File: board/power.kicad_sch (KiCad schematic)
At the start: 10 parts, among them U1 OKI-78SR-5_1.5-W36H-C

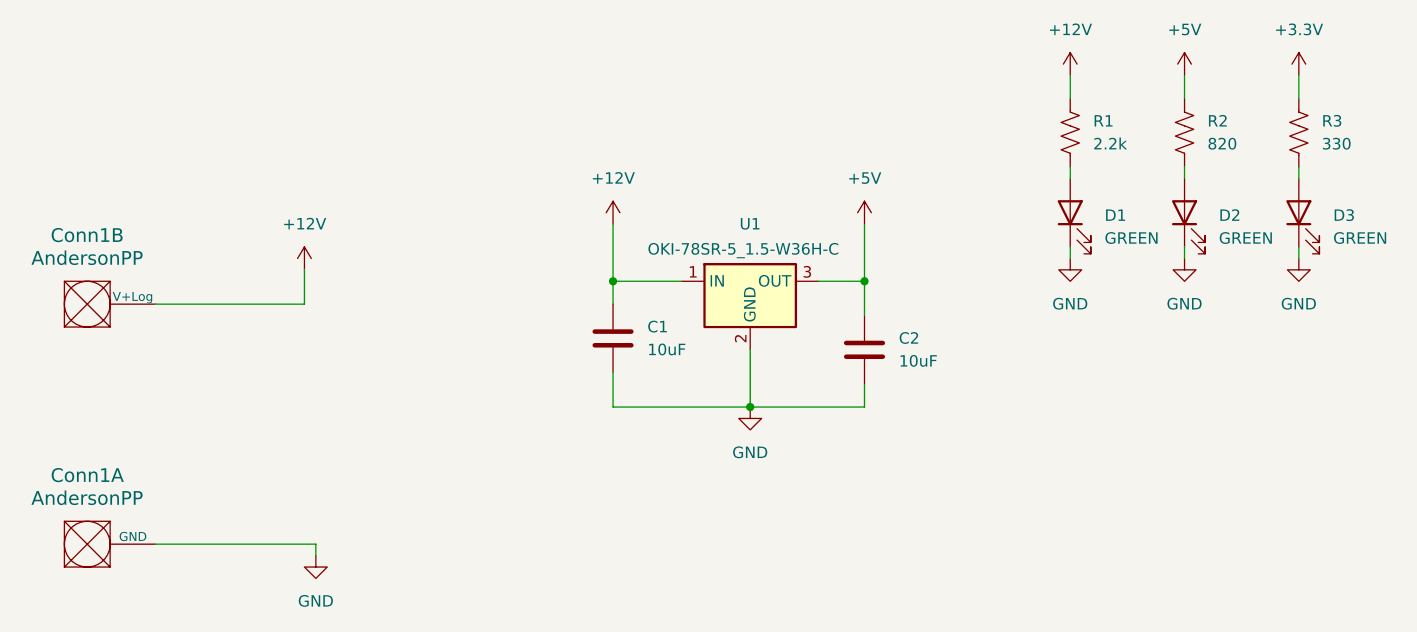
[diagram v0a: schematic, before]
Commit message: Added Servo, cleaned up schematic
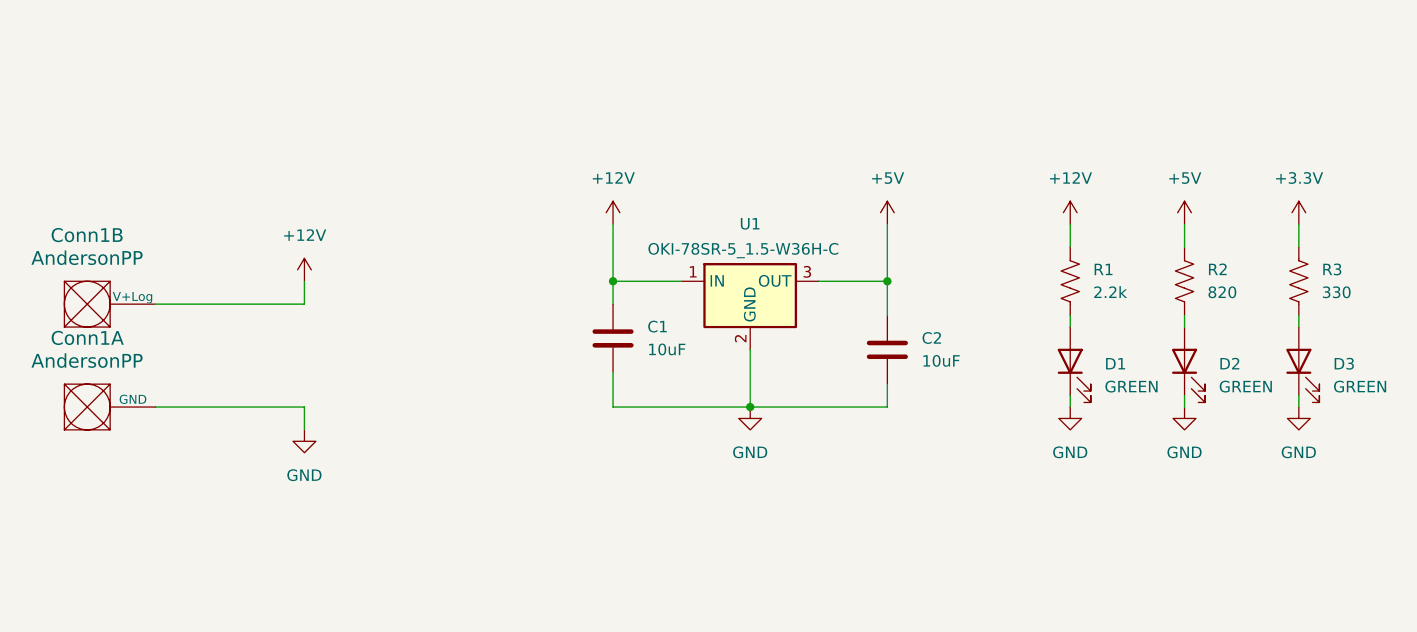
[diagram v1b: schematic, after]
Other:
- moved on the sheet: C2, Conn1A, D1, D2, D3, R1, R2, R3

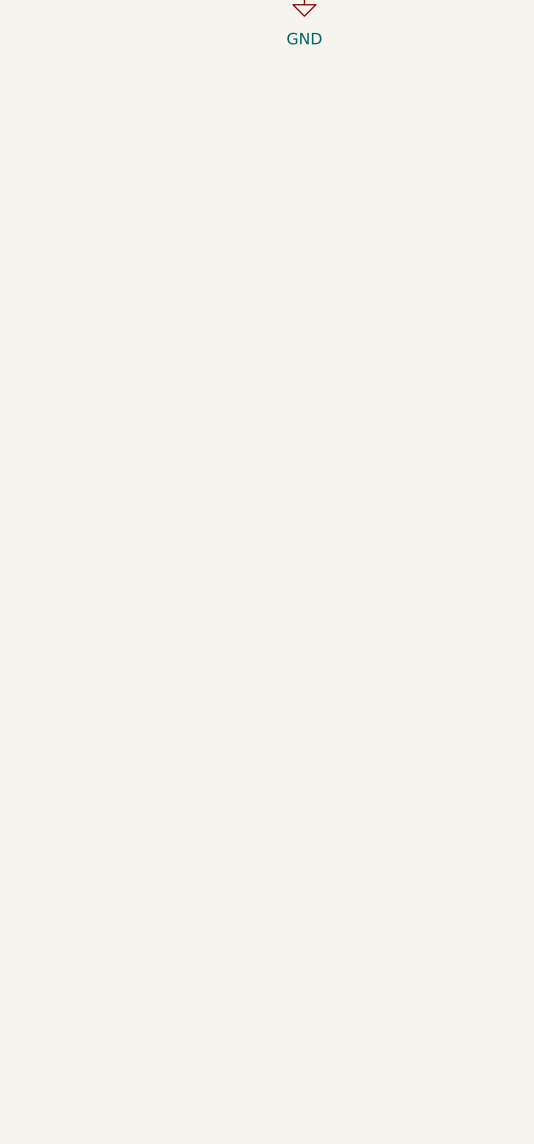
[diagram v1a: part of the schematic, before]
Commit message: Moved things to make more sense
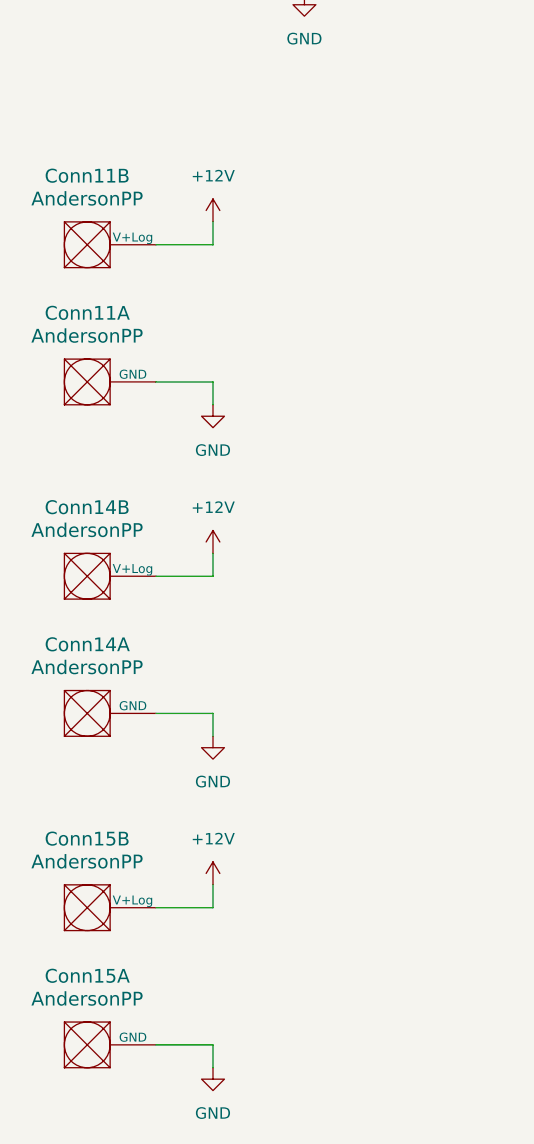
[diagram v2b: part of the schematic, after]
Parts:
- added Conn11, Conn14, Conn15: AndersonPP, symbol MRDT_Connectors:AndersonPP
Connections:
- net +12V: now also Conn11.2 (V+Log), Conn14.2 (V+Log), Conn15.2 (V+Log)
- net GND: now also Conn11.1 (GND), Conn14.1 (GND), Conn15.1 (GND)

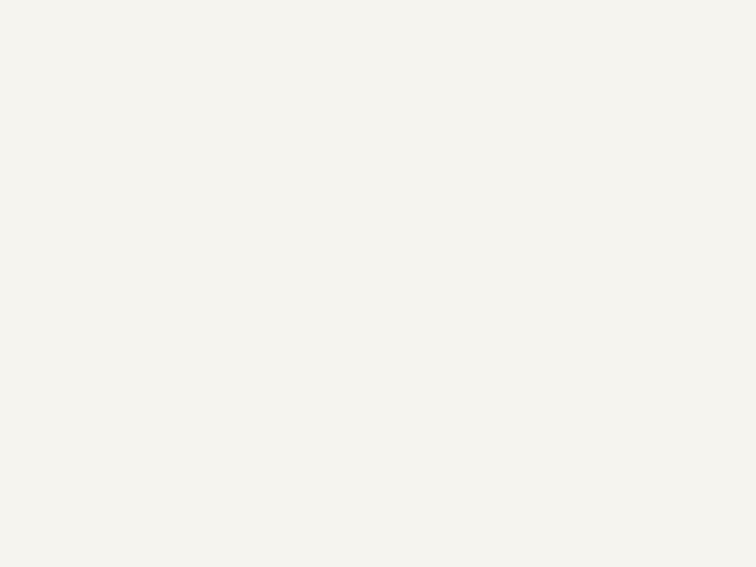
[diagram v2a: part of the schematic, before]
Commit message: Soil sensors pt. 2
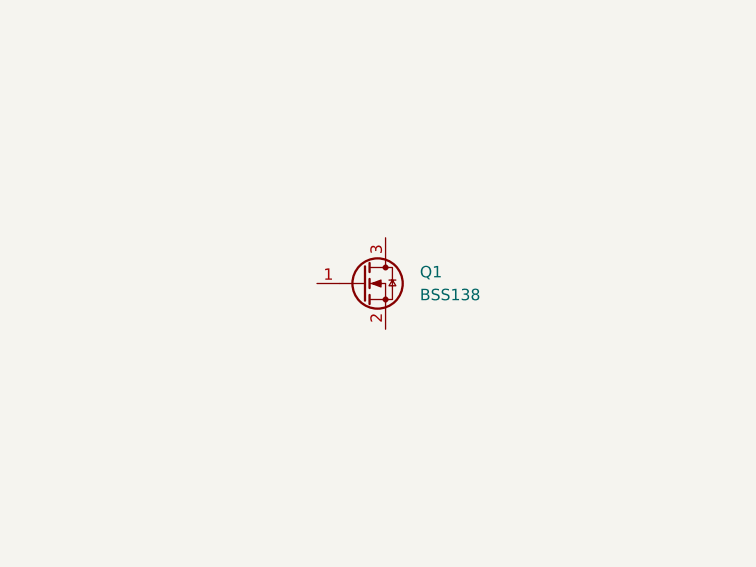
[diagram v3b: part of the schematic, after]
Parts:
- added Q1: BSS138, Package_TO_SOT_SMD:SOT-23, symbol Transistor_FET:BSS138
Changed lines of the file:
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@@
+	)
+	(symbol
+		(lib_id "Transistor_FET:BSS138")
+		(at 134.62 111.76 0)
+		(unit 1)
+		(exclude_from_sim no)
+		(in_bom yes)
+		(on_board yes)
+		(dnp no)
+		(fields_autoplaced yes)
+		(property "Reference" "Q1"
+			(at 140.97 110.4899 0)
+			(effects
+				(font
+					(size 1.27 1.27)
+				)
+				(justify left)
+			)
+		)
+		(property "Value" "BSS138"
+			(at 140.97 113.0299 0)
+			(effects
+				(font
+					(size 1.27 1.27)
+				)
+				(justify left)
+			)
+		)
+		(property "Footprint" "Package_TO_SOT_SMD:SOT-23"
+			(at 139.7 113.665 0)
+			(effects
+				(font
+					(size 1.27 1.27)
+					(italic yes)
+				)
+				(justify left)
+				(hide yes)
+			)
+		)
+		(property "Datasheet" "https://www.onsemi.com/pub/Collateral/BSS138-D.PDF"
+			(at 139.7 115.57 0)
+			(effects
+				(font
+					(size 1.27 1.27)
+				)
+				(justify left)
+				(hide yes)
+			)
+		)
+		(property "Description" "50V Vds, 0.22A Id, N-Channel MOSFET, SOT-23"
+			(at 134.62 111.76 0)
+			(effects
+				(font
+					(size 1.27 1.27)
+				)
+				(hide yes)
+			)
+		)
+		(pin "3"
+		)
+		(pin "2"
+		)
+		(pin "1"
+		)
+		(instances
+			(project ""
+				(path "/05fd3c2e-b986-4426-9c38-2a77d5c929de/3b4d7bd3-b617-4540-8dc9-414a3afad923"
+					(reference "Q1")
+					(unit 1)
+				)
+			)
+		)
 	)
 	(symbol

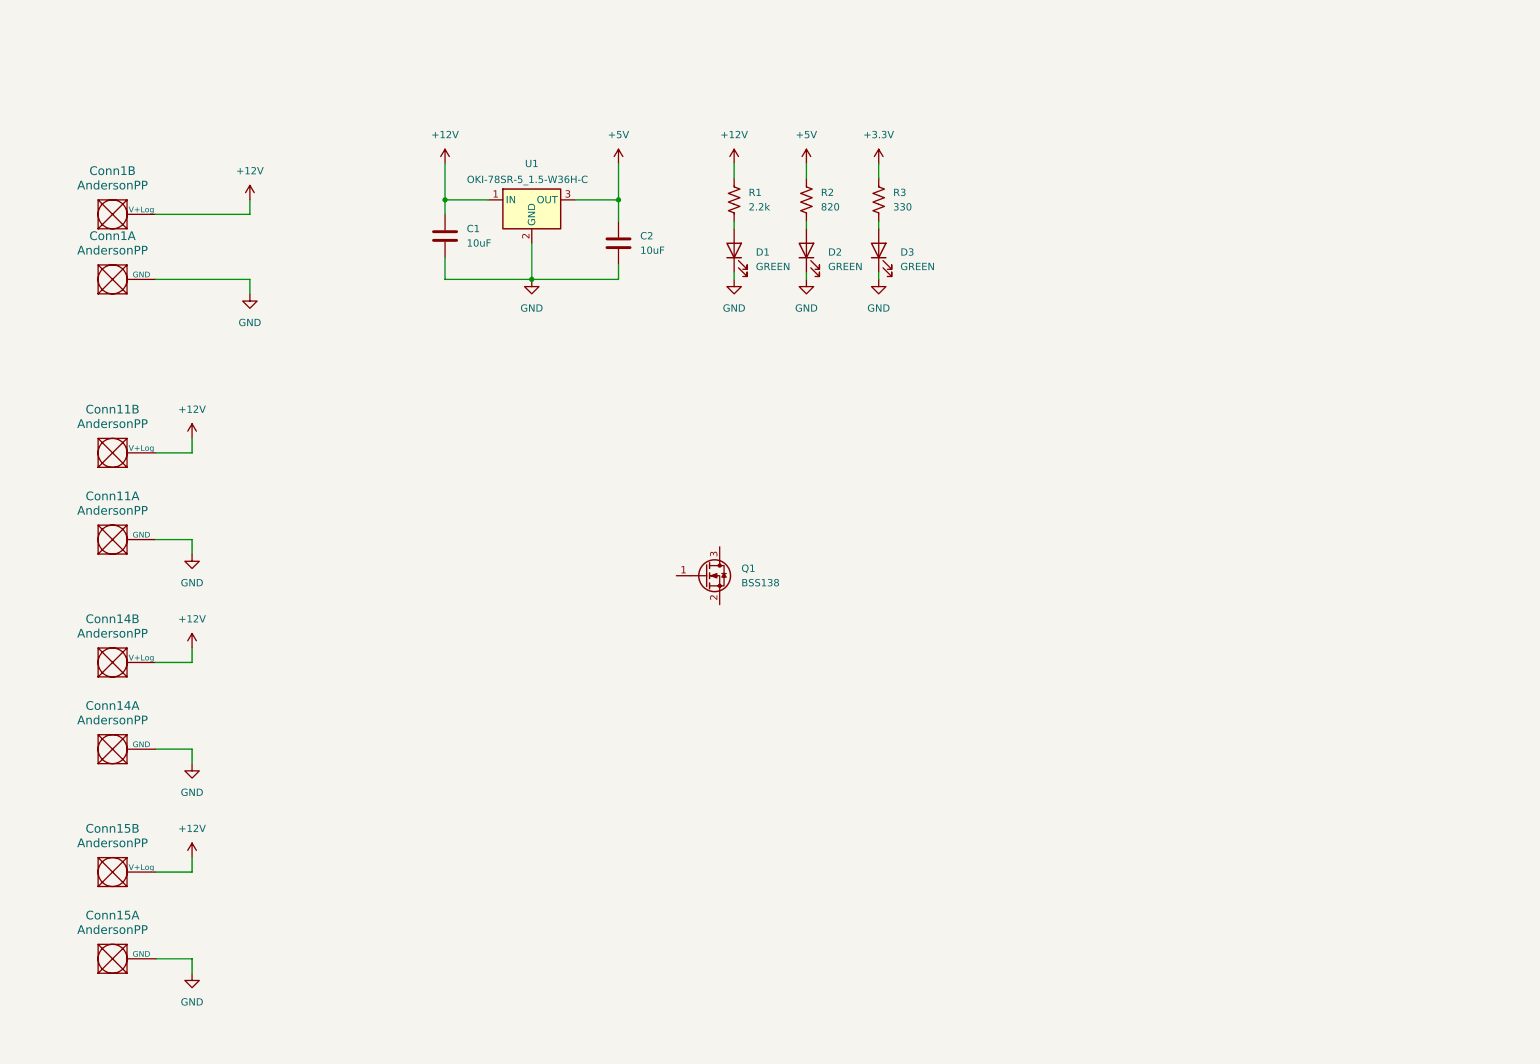
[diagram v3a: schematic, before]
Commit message: Added Labels, Missing Requirements, and Refined Look
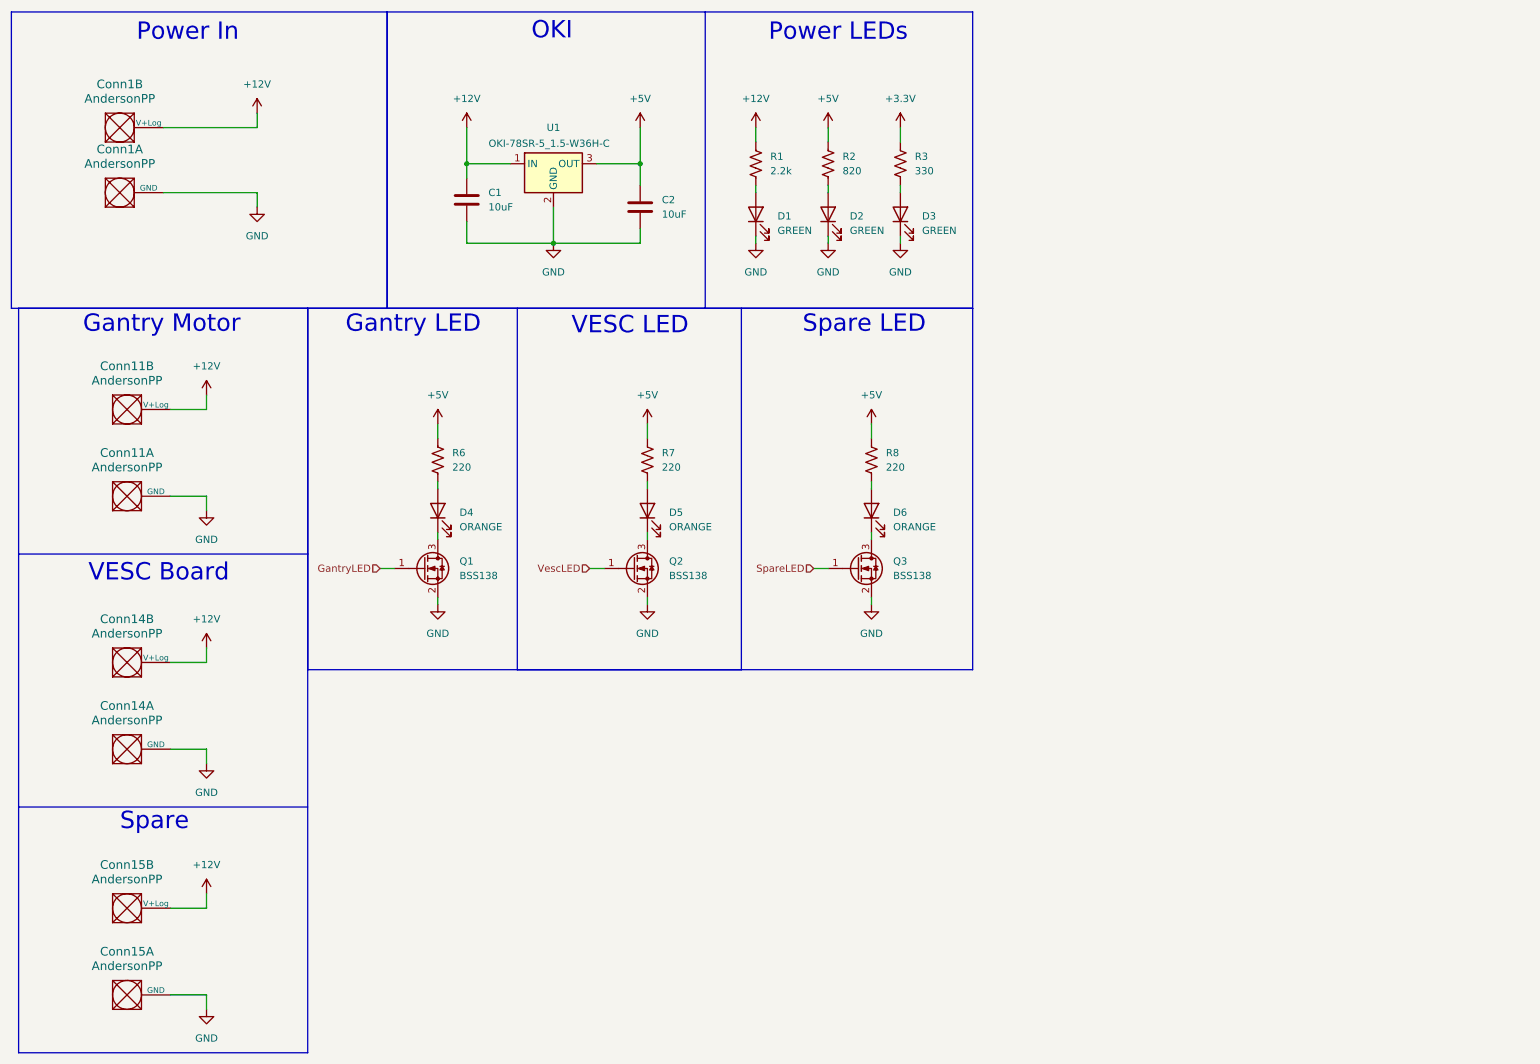
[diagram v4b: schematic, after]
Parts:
- added D4, D5, D6: ORANGE, symbol Device:LED
- added Q2, Q3: BSS138, Package_TO_SOT_SMD:SOT-23, symbol Transistor_FET:BSS138
- added R6, R7, R8: 220, symbol Device:R_US
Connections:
- net +5V: now also R6.1, R7.1, R8.1
- net GND: now also Q1.2 (S), Q2.2 (S), Q3.2 (S)
- net GantryLED: now reaches Q1.1 (G)
- net at Q1.3 (D): now also D4.1 (K)
- new net: D4.2 (A), R6.2
- new net: D5.1 (K), Q2.3 (D)
- new net: D6.1 (K), Q3.3 (D)
- new net: D6.2 (A), R8.2
- new net: D5.2 (A), R7.2
- new net SpareLED: Q3.1 (G)
- new net VescLED: Q2.1 (G)
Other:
- note added: "Gantry LED"
- note added: "Gantry Motor"
- note added: "OKI"
- note added: "Power In"
- note added: "Power LEDs"
- note added: "Spare"
- note added: "Spare LED"
- note added: "VESC Board"
- note added: "VESC LED"
- moved on the sheet: C1, C2, Conn11A, Conn11B, Conn14A, Conn14B, Conn15A, Conn15B, Conn1A, Conn1B, D1, D2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

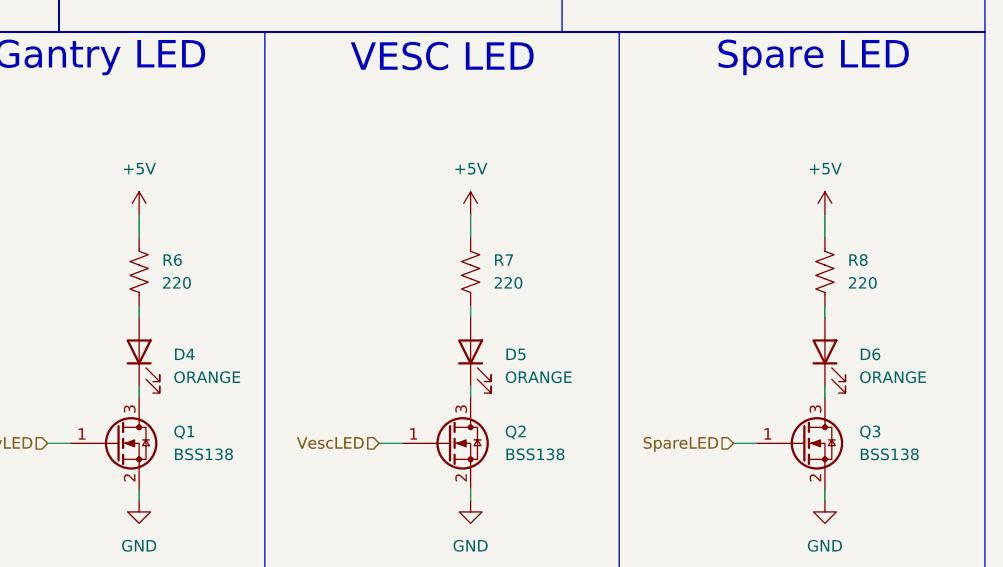
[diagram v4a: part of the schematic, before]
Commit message: Adjusted resistor values & renamed AF outputs
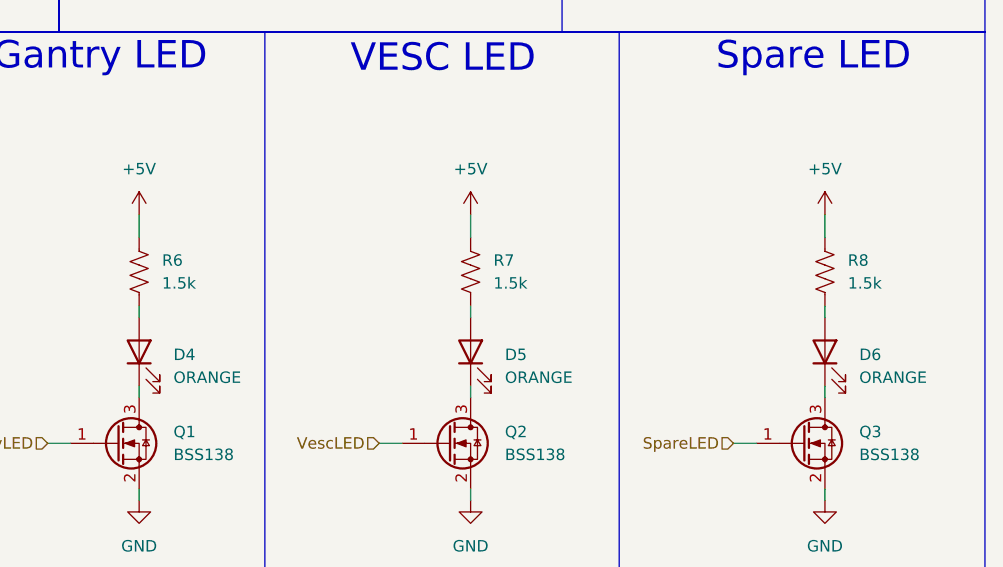
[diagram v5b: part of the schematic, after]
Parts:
- R6, R7, R8: value 220 -> 1.5k
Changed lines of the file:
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@@
 			)
 		)
-		(property "Value" "220"
+		(property "Value" "1.5k"
 			(at 127 92.7099 0)
 			(effects
@@
 			)
 		)
-		(property "Value" "220"
+		(property "Value" "1.5k"
 			(at 90.17 92.7099 0)
 			(effects
@@
 			)
 		)
-		(property "Value" "220"
+		(property "Value" "1.5k"
 			(at 166.37 92.7099 0)
 			(effects
